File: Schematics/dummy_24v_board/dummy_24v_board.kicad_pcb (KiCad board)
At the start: 2 copper layers, 69.5 x 60 mm, 11 parts, among them J1 Stack Male Edge Connector, J2 Conn_01x02_Socket, J3 Conn_01x02_Socket, J4 Conn_01x02_Socket, J5 Conn_01x02_Socket

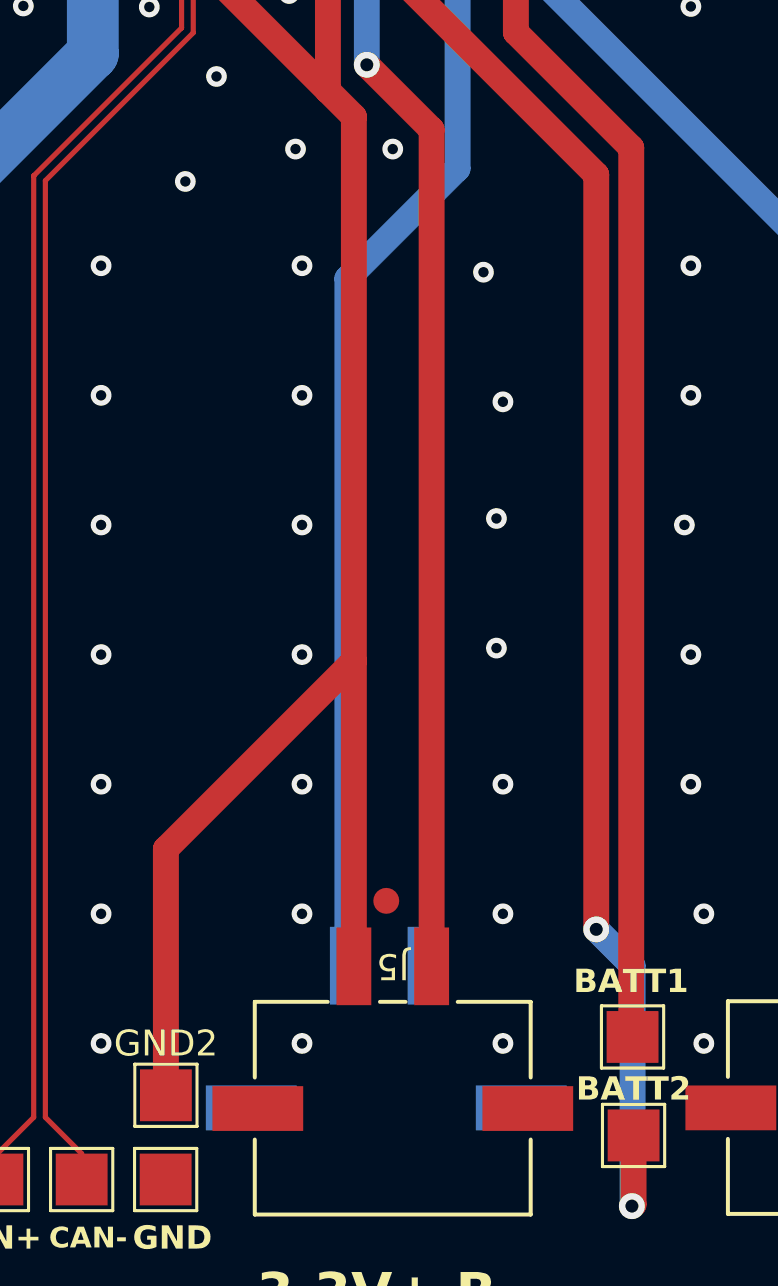
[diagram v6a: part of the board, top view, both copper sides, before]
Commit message: shifted 5V molex
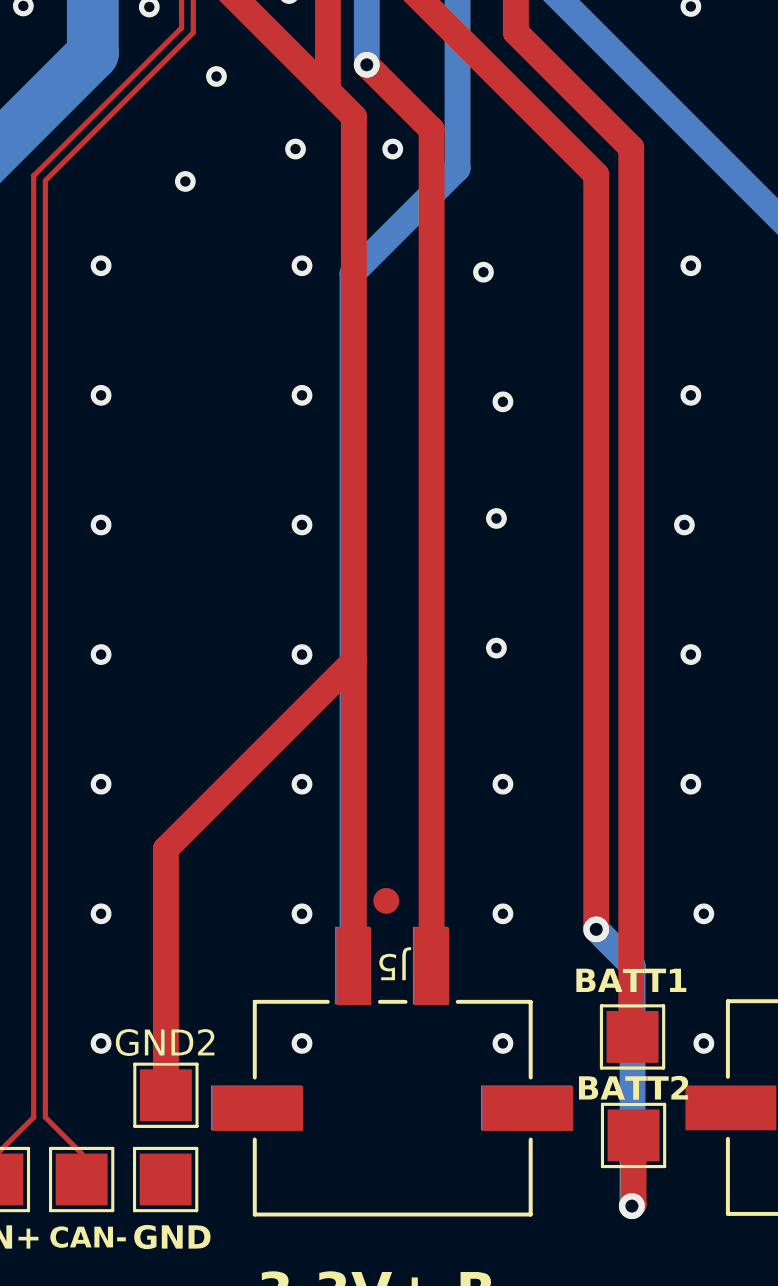
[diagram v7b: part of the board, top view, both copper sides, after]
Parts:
- moved J4 0.20 mm to (58.7, 67.5)
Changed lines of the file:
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@@
 		)
 		(property "Footprint" "footprints:CONN_2-1445057-2_TYCO"
-			(at 0 0 360)
+			(at 0 0 0)
 			(layer "F.Fab")
 			(hide yes)
@@
 		)
 		(property "Datasheet" ""
-			(at 0 0 360)
+			(at 0 0 0)
 			(layer "F.Fab")
 			(hide yes)
@@
 		)
 		(property "Description" "Generic connector, single row, 01x02, script generated"
-			(at 0 0 360)
+			(at 0 0 0)
 			(layer "F.Fab")
 			(hide yes)
@@
 	(footprint "footprints:CONN_2-1445057-2_TYCO"
 		(layer "B.Cu")
-		(at 58.5 67.5)
+		(at 58.7 67.5)
 		(tags "2-1445057-2 ")
 		(property "Reference" "J4"
@@
 		)
 	)
-	(gr_text_box "Move connectors back to 4mm line, \nuse ground plane for GND but use trace for GND2, \nconsider move 3.3V_B to the top so we don't need to cross traces\nand of fix all netclasses so design rule checker doesn't fail"
-		(start 100 31.2)
-		(end 172.9 51.1)
-		(layer "F.Cu")
-		(effects
-			(font
-				(size 1.5 1.5)
-				(thickness 0.3)
-				(bold yes)
-			)
-			(justify left top)
-		)
-		(border yes)
-		(stroke
-			(width 0.2)
-			(type solid)
-		)
-	)
 	(segment
 		(start 80 67.499999)
@@
 	)
 	(segment
-		(start 58.5 41)
-		(end 58.5 67.5)
-		(width 1)
+		(start 62.83 26)
+		(end 62.83 22.57)
+		(width 0.5)
 		(layer "B.Cu")
 		(net 3)
 	)
 	(segment
-		(start 62.75 26.42)
-		(end 62.75 36.75)
+		(start 58.7 40.8)
+		(end 58.7 67.5)
 		(width 1)
 		(layer "B.Cu")
@@
 	)
 	(segment
-		(start 62.83 26)
-		(end 62.83 22.57)
+		(start 63 26.17)
+		(end 63.83 25.34)
 		(width 0.5)
 		(layer "B.Cu")
@@
 	)
 	(segment
-		(start 63 26.17)
-		(end 63.83 25.34)
-		(width 0.5)
+		(start 62.75 26.42)
+		(end 62.75 36.75)
+		(width 1)
 		(layer "B.Cu")
 		(net 3)
@@
 	)
 	(segment
-		(start 63 26.17)
-		(end 62.83 26)
-		(width 0.5)
+		(start 62.75 36.75)
+		(end 58.7 40.8)
+		(width 1)
 		(layer "B.Cu")
 		(net 3)
 	)
 	(segment
-		(start 62.75 36.75)
-		(end 58.5 41)
-		(width 1)
+		(start 63 26.17)
+		(end 62.83 26)
+		(width 0.5)
 		(layer "B.Cu")
 		(net 3)
@@
 		(net 7)
 		(net_name "GND")
-		(layers "F&B.Cu")
+		(layers "F.Cu" "B.Cu")
 		(hatch edge 0.5)
 		(connect_pads yes
